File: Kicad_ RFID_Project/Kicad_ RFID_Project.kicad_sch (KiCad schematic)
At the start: 0 parts

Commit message: ajout schéma Kicad
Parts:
- added BZ1: Buzzer, symbol Device:Buzzer
- added C1: 10u, symbol Device:C
- added C2: 22u, symbol Device:C_Polarized
- added C3: 100n, symbol Device:C
- added D1, D2: LED, symbol Device:LED
- added J1: Conn_01x08, symbol Connector_Generic:Conn_01x08
- added J2: Conn_ST_STDC14, symbol Connector:Conn_ST_STDC14
- added J3: USB_C_Receptacle_USB2.0_14P, symbol Connector:USB_C_Receptacle_USB2.0_14P
- added R1, R2: 22, symbol Device:R
- added R3, R4: 5.1k, symbol Device:R
- added R5: 3k, symbol Device:R
- added R6: 1.5k, symbol Device:R
- added SW1: RESET, symbol Switch:SW_Push
- added U1: STM32L476RGTx, Package_QFP:LQFP-64_10x10mm_P0.5mm, symbol MCU_ST_STM32L4:STM32L476RGTx
- added U2: AZ1117CH2-3.3, Package_TO_SOT_SMD:SOT-223-3_TabPin2, symbol Regulator_Linear:AZ1117CH2-3.3
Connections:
- new net: D2.2 (A), R6.1
- new net: J3.B5 (CC2), R3.1
- new net: J3.A6 (D+), J3.B6 (D+), R2.2
- new net: U1.18 (VSS), U1.31 (VSS), U1.47 (VSS), U1.63 (VSS)
- new net: D1.2 (A), R5.1
- new net: J3.A7 (D-), J3.B7 (D-), R1.1
- new net: J3.A5 (CC1), R4.1
- new net +3.3V: C2.1, J1.8 (Pin_8), J2.3 (VCC), R6.2, U2.3 (OUT)
- new net +5V: C1.1, J3.A4 (VBUS), J3.A9 (VBUS), J3.B4 (VBUS), J3.B9 (VBUS), R5.2, U2.1 (IN)
- new net BUZZ: BZ1.1 (+), U1.41 (PA8)
- new net GND: BZ1.2 (-), C1.2, C2.2, C3.2, D1.1 (K), D2.1 (K), J1.6 (Pin_6), J2.11 (GNDDetect), J2.5 (GND), J2.7 (GND), J3.A1 (GND), J3.A12 (GND), J3.B1 (GND), J3.B12 (GND), R3.2, R4.2, SW1.2, U2.2 (GND)
- new net NRST: C3.1, J2.12 (~{RST}), SW1.1, U1.7 (NRST)
- new net SPI2_MISO: J1.4 (Pin_4), U1.10 (PC2)
- new net SPI2_MOSI: J1.3 (Pin_3), U1.11 (PC3)
- new net SPI2_RST: J1.7 (Pin_7), U1.23 (PA7)
- new net SPI2_SCK: J1.2 (Pin_2), U1.29 (PB10)
- new net SPI2_SDA: J1.1 (Pin_1), U1.33 (PB12)
- new net SWCLK: J2.4 (JTMS/SWDIO), J2.6 (JCLK/SWCLK), J2.8 (JTDO/SWO), U1.46 (PA13), U1.49 (PA14), U1.55 (PB3)
- new net USART2_RX: J2.13 (VCP_RX), J2.14 (VCP_TX), U1.16 (PA2), U1.17 (PA3)
- new net USB_DM: R1.2, U1.44 (PA11)
- new net USB_DP: R2.1, U1.45 (PA12)
- no-connect marks 0 -> 4
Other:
- note added: "Connecteur SPI + STlink"
- note added: "LEDs Témoin alim"
- note added: "Processeur"
- company: (none) -> ENSEA
- title: (none) -> PCB-RFID-Project

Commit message: changement kicad
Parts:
- added C10, C5, C6, C7, C8, C9: 100n, Capacitor_SMD:C_0402_1005Metric, symbol Device:C
- added C26: 4u7, Capacitor_SMD:C_0402_1005Metric, symbol Device:C
- added R7: 10k, symbol Device:R
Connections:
- net +3.3V: now also U1.1 (VBAT), U1.13 (VDDA), U1.19 (VDD), U1.32 (VDD), U1.48 (VDDUSB), U1.64 (VDD), C10.2, C26.2, C5.2, C6.2, C7.2, C8.2, C9.2
- net GND: now also U1.12 (VSSA), U1.18 (VSS), U1.31 (VSS), U1.47 (VSS), U1.63 (VSS), C10.1, C26.1, C5.1, C6.1, C7.1, C8.1, C9.1, R7.1
- net SWCLK: no longer J2.4 (JTMS/SWDIO), J2.8 (JTDO/SWO), U1.46 (PA13), U1.55 (PB3)
- net USART2_RX: no longer J2.13 (VCP_RX), U1.16 (PA2)
- net at U1.60 (BOOT0): now also R7.2
- new net SWDIO: J2.4 (JTMS/SWDIO), U1.46 (PA13)
- new net SWO: J2.8 (JTDO/SWO), U1.55 (PB3)
- new net USART2_TX: J2.13 (VCP_RX), U1.16 (PA2)
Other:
- note added: "Régulateur 3.3V"
- note removed: "LEDs Témoin alim"
- moved on the sheet: C3, J2, SW1, U1

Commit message: ajout trous de fixation kicad
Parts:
- added H1, H2, H3, H4, H5, H6, H7, H8: MountingHole, symbol Mechanical:MountingHole
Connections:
- no-connect marks 4 -> 42
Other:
- note added: "Buzzer"
- note added: "Connecteur USB-C"
- note added: "LEDs Alim"
- note added: "Trous de fixation"
- moved on the sheet: BZ1, D1, D2, R5, R6

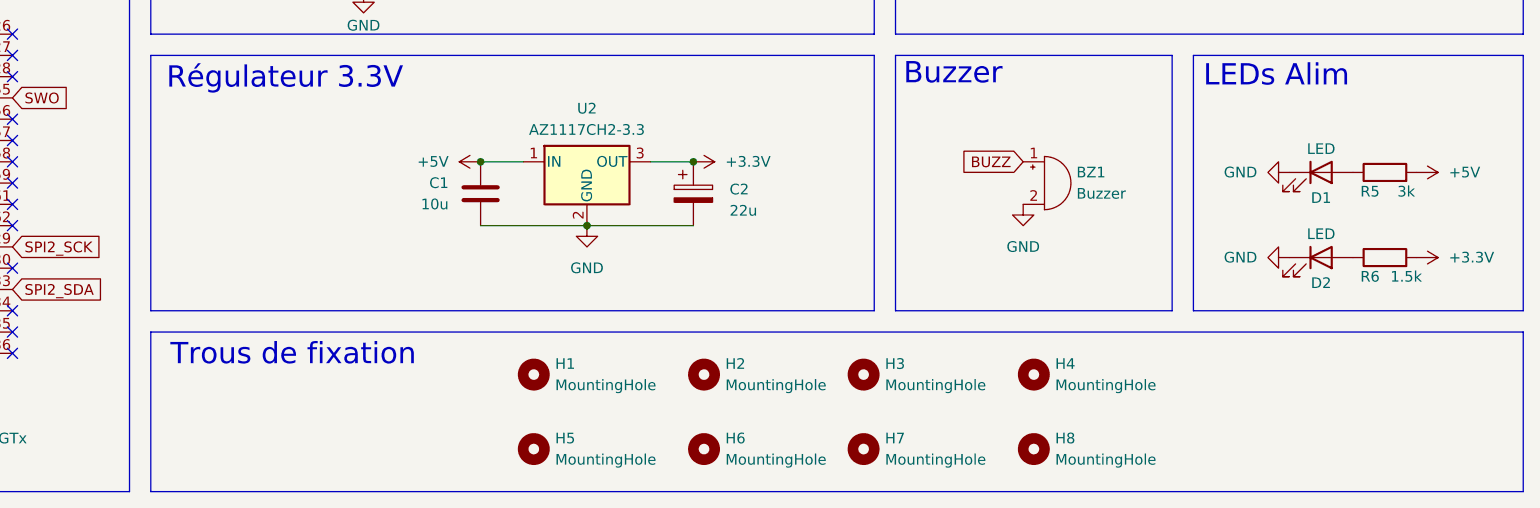
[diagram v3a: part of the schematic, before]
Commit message: ajout mounting holes et powerflag
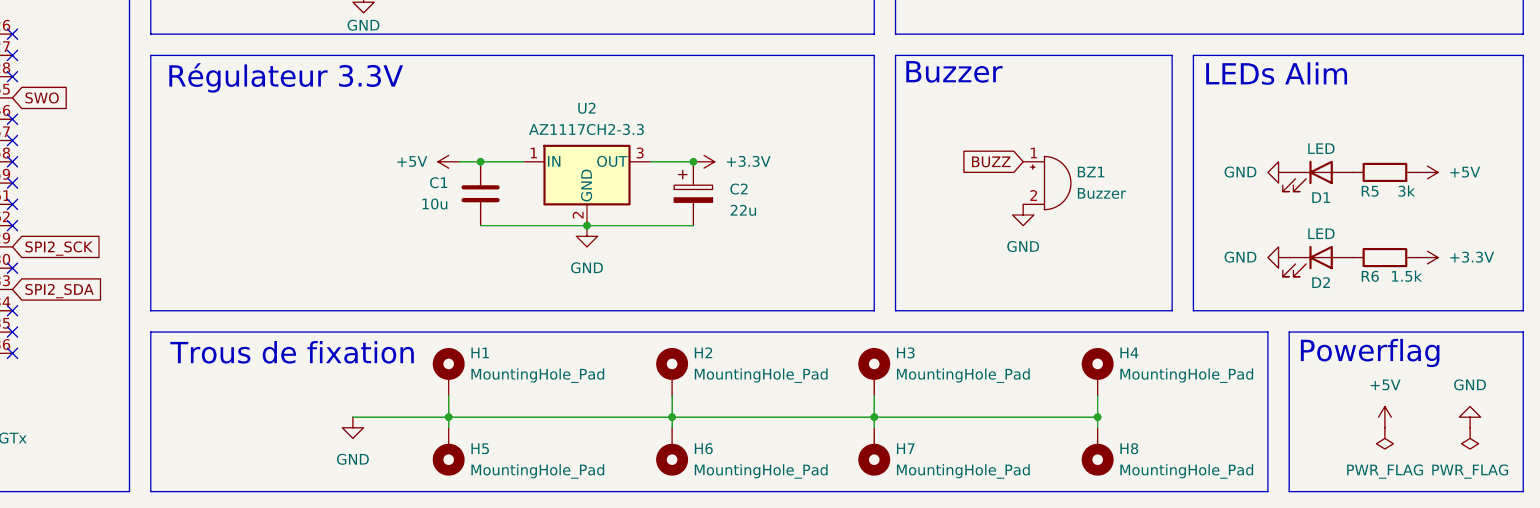
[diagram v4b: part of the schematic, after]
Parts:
- removed H1, H2, H3, H4, H5, H6, H7, H8: MountingHole, symbol Mechanical:MountingHole
- added H1, H2, H3, H4, H5, H6, H7, H8: MountingHole_Pad, symbol Mechanical:MountingHole_Pad
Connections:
- net GND: now also H1.1, H2.1, H3.1, H4.1, H5.1, H6.1, H7.1, H8.1
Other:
- note added: "Powerflag"

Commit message: derniers details schéma + début routage
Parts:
- removed H5, H6, H7, H8: MountingHole_Pad, symbol Mechanical:MountingHole_Pad
- removed J3: USB_C_Receptacle_USB2.0_14P, symbol Connector:USB_C_Receptacle_USB2.0_14P
- added D3: LED, LED_SMD:LED_0603_1608Metric, symbol Device:LED
- added J3: 10172013-00011LF, 10172013-00011LF:AMPHENOL_10172013-00011LF, symbol 10172013-00011LF:10172013-00011LF
- added Q1: 2N3904, Package_TO_SOT_THT:TO-92_Inline, symbol Transistor_BJT:2N3904
- added R8: 1k, Resistor_SMD:R_0603_1608Metric, symbol Device:R
- added R9: 1.5k, Resistor_SMD:R_0603_1608Metric, symbol Device:R
- BZ1: footprint (none) -> Buzzer_Beeper:Buzzer_D14mm_H7mm_P10mm
- C1, C3: footprint (none) -> Capacitor_SMD:C_0603_1608Metric
- C10, C5, C6, C7, C8, C9: footprint Capacitor_SMD:C_0402_1005Metric -> Capacitor_SMD:C_0603_1608Metric
- C2: footprint (none) -> Capacitor_SMD:CP_Elec_5x5.4
- C4: renamed from C26; footprint Capacitor_SMD:C_0402_1005Metric -> Capacitor_SMD:C_0603_1608Metric
- D1, D2: footprint (none) -> LED_SMD:LED_0603_1608Metric
- H1, H2, H3, H4: footprint (none) -> MountingHole:MountingHole_3.2mm_M3_DIN965_Pad
- J1: footprint (none) -> CEG006900:MODULE_CEG006900
- J2: footprint (none) -> Connector_PinHeader_1.27mm:PinHeader_2x07_P1.27mm_Vertical_SMD
- R1, R2, R3, R4, R5, R6, R7: footprint (none) -> Resistor_SMD:R_0603_1608Metric
- SW1: footprint (none) -> Button_Switch_SMD:SW_SPST_PTS645Sx43SMTR92
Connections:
- net +3.3V: now also BZ1.1 (+), J1.1 (Pin_1); no longer J1.8 (Pin_8)
- net +5V: now also J3.A4_B9 (VBUS), J3.A9_B4 (VBUS)
- net BUZZ: now also R8.1; no longer BZ1.1 (+)
- net GND: now also J1.3 (Pin_3), R4.1, D3.1 (K), J3.A12_B1 (GND), J3.A1_B12 (GND), Q1.1 (E); no longer BZ1.2 (-), J1.6 (Pin_6), R4.2
- net SPI2_MISO: now also J1.5 (Pin_5); no longer J1.4 (Pin_4)
- net SPI2_MOSI: now also J1.6 (Pin_6); no longer J1.3 (Pin_3)
- net SPI2_RST: now also J1.2 (Pin_2), U1.15 (PA1); no longer J1.7 (Pin_7), U1.23 (PA7)
- net SPI2_SCK: now also J1.7 (Pin_7); no longer J1.2 (Pin_2)
- net SPI2_SDA: now also J1.8 (Pin_8), U1.14 (PA0); no longer J1.1 (Pin_1), U1.33 (PB12)
- net at R3.1: now also J3.B5 (CC2)
- net D+: now reaches R2.2
- net D+: now also J3.A6 (DP1), J3.B6 (DP2)
- net USER_LED: now reaches U1.40 (PC9)
- net USER_LED: now also R9.2
- net D-: now reaches R1.1
- net D-: now also J3.A7 (DN1), J3.B7 (DN2)
- new net: BZ1.2 (-), Q1.3 (C)
- new net: Q1.2 (B), R8.2
- new net: D3.2 (A), R9.1
- new net: J3.A5 (CC1), R4.2
- new net: J3.SH1 (SHIELD), J3.SH2 (SHIELD), J3.SH3 (SHIELD), J3.SH4 (SHIELD)
- no-connect marks 42 -> 43
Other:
- note added: "LED Utilisateur"
- note removed: "LEDs Alim"
- moved on the sheet: BZ1, C1, C2, C3, D1, D2, R1, R2, R3, R4, R5, R6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

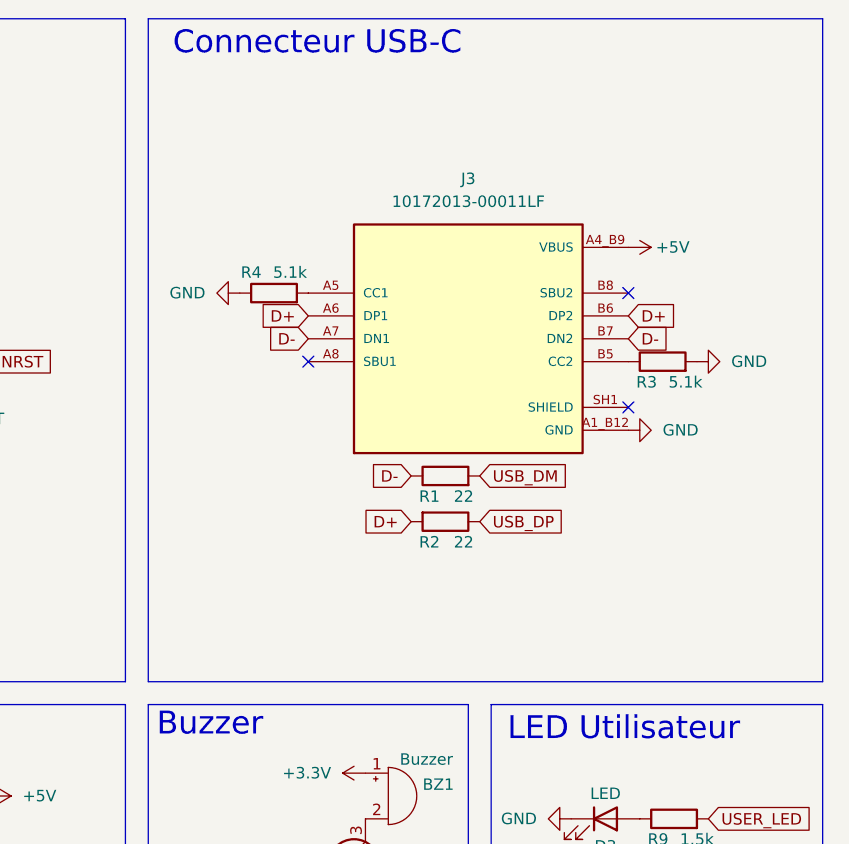
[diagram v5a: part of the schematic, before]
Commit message: ajout des leds electrostatiques pour l'USB-C
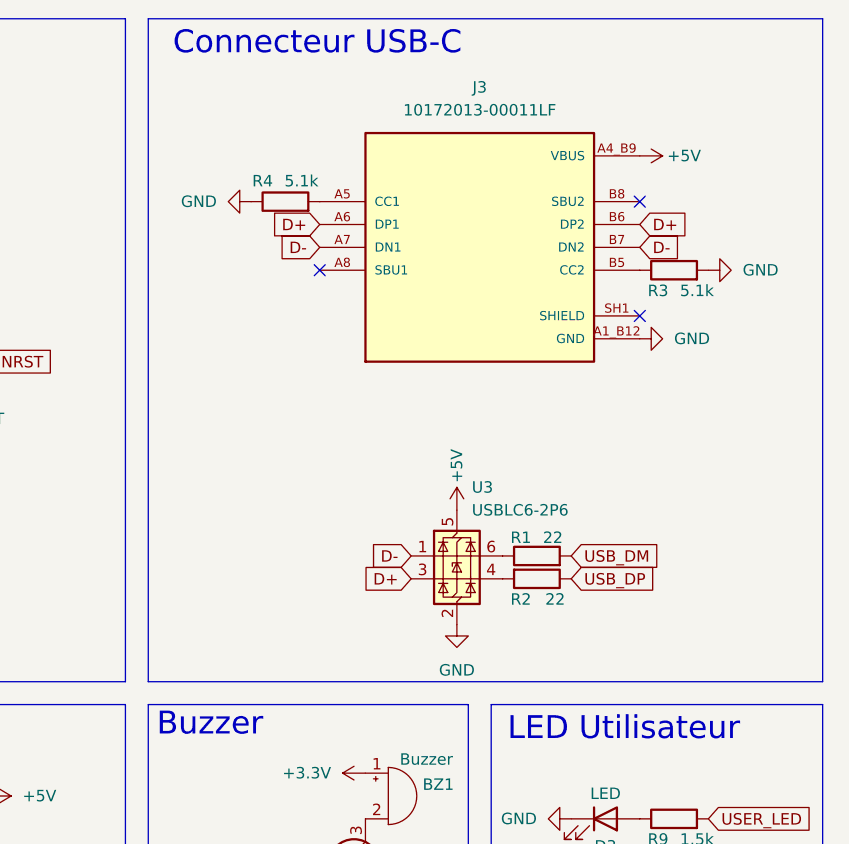
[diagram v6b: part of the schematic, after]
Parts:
- added U3: USBLC6-2P6, Package_TO_SOT_SMD:SOT-666, symbol Power_Protection:USBLC6-2P6
- BZ1: MPN (none) -> PS1420P02CT
- C1: MPN (none) -> GRM188R61A106KE69D
- C10, C3, C5, C6, C7, C8, C9: MPN (none) -> GRM188R71C104KA01D
- C2: MPN (none) -> GRM21BR61A226ME44L
- C4: MPN (none) -> GRM188R61A475KE15D
- D1, D2, D3: MPN (none) -> 150060RS75000
- J1: MPN (none) -> 61300811121
- J2: MPN (none) -> STDC14
- J3: MPN (none) -> 10172013-00011LF
- Q1: MPN (none) -> 2N3904BU
- R1, R2, R3, R4: MPN (none) -> RC0603FR-0722RL
- R5: MPN (none) -> RC0603FR-073KL
- R6, R9: MPN (none) -> RC0603FR-071K5L
- R7: MPN (none) -> RC0603FR-0710KL
- R8: MPN (none) -> RC0603FR-071KL
- SW1: MPN (none) -> PTS645SK43SMTR92 LFS
- U1: MPN (none) -> STM32L476RGT6
- U2: MPN (none) -> AZ1117CH2-3.3TRG1
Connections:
- net +5V: now also U3.5 (VBUS)
- net D+: now also U3.3 (I/O2); no longer R2.2
- net D-: now also U3.1 (I/O1); no longer R1.1
- net GND: now also U3.2 (GND)
- new net: R2.2, U3.4 (I/O2)
- new net: R1.1, U3.6 (I/O1)
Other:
- moved on the sheet: J3, R1, R2, R3, R4
